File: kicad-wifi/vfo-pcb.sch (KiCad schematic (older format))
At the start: 89 parts, among them J1 Rotery Encoder1, J10 Link-out 1-2, J11 Link-out 1-0, J12 Link-out 2-0, J13 Link-out 2-2, J14 Link-out 2-1, J15 Link-out 1-1, J2 Rotery Encoder2, J3 Analog in 3-6, J4 RxTx, J5 V12, J6 ESP32L, J7 ESP32R, J8 ILI9341, J9 Conn_01x07_Female, Q1 BFR92, Q2 BFR92, Q3 BFR92, Q4 BFR92, Q5 BFR92, Q6 BFR92, SW1 Rotary_Encoder_Switch, U1 AMS1117, U2 LM2576HVS-ADJ, U3 Si5351A-B-GT, U4 Si5351A-B-GT, Y1 Crystal, Y2 Crystal

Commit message: update wifi pcb
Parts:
- removed R21, R22, R23, R24, R25, R29: 150, Resistor_SMD:R_1206_3216Metric_Pad1.42x1.75mm_HandSolder, symbol Device:R
- added C20, C21, C22, C23, C24, C25: 100n, Capacitor_SMD:C_1206_3216Metric_Pad1.42x1.75mm_HandSolder, symbol Device:C
- R26, R27, R31: value 33 -> 200
- R33, R34, R37: value 150 -> 68
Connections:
- net at R26.2, R33.1: now also C23.1; no longer J12.1 (In)
- net at R31.2, R37.1: now also C24.1; no longer J14.1 (In)
- net at R28.2, R32.1: now also C20.1; no longer J11.1 (In)
- net at R35.2, R38.1: now also C21.1; no longer J15.1 (In)
- net at R30.2, R36.1: now also C22.1; no longer J10.1 (In)
- net at R27.2, R34.1: now also C25.1; no longer J13.1 (In)
- new net: C23.2, J12.1 (In)
- new net: C24.2, J14.1 (In)
- new net: C20.2, J11.1 (In)
- new net: C21.2, J15.1 (In)
- new net: C22.2, J10.1 (In)
- new net: C25.2, J13.1 (In)
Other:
- moved on the sheet: J10, J11, J12, J13, J14, J15

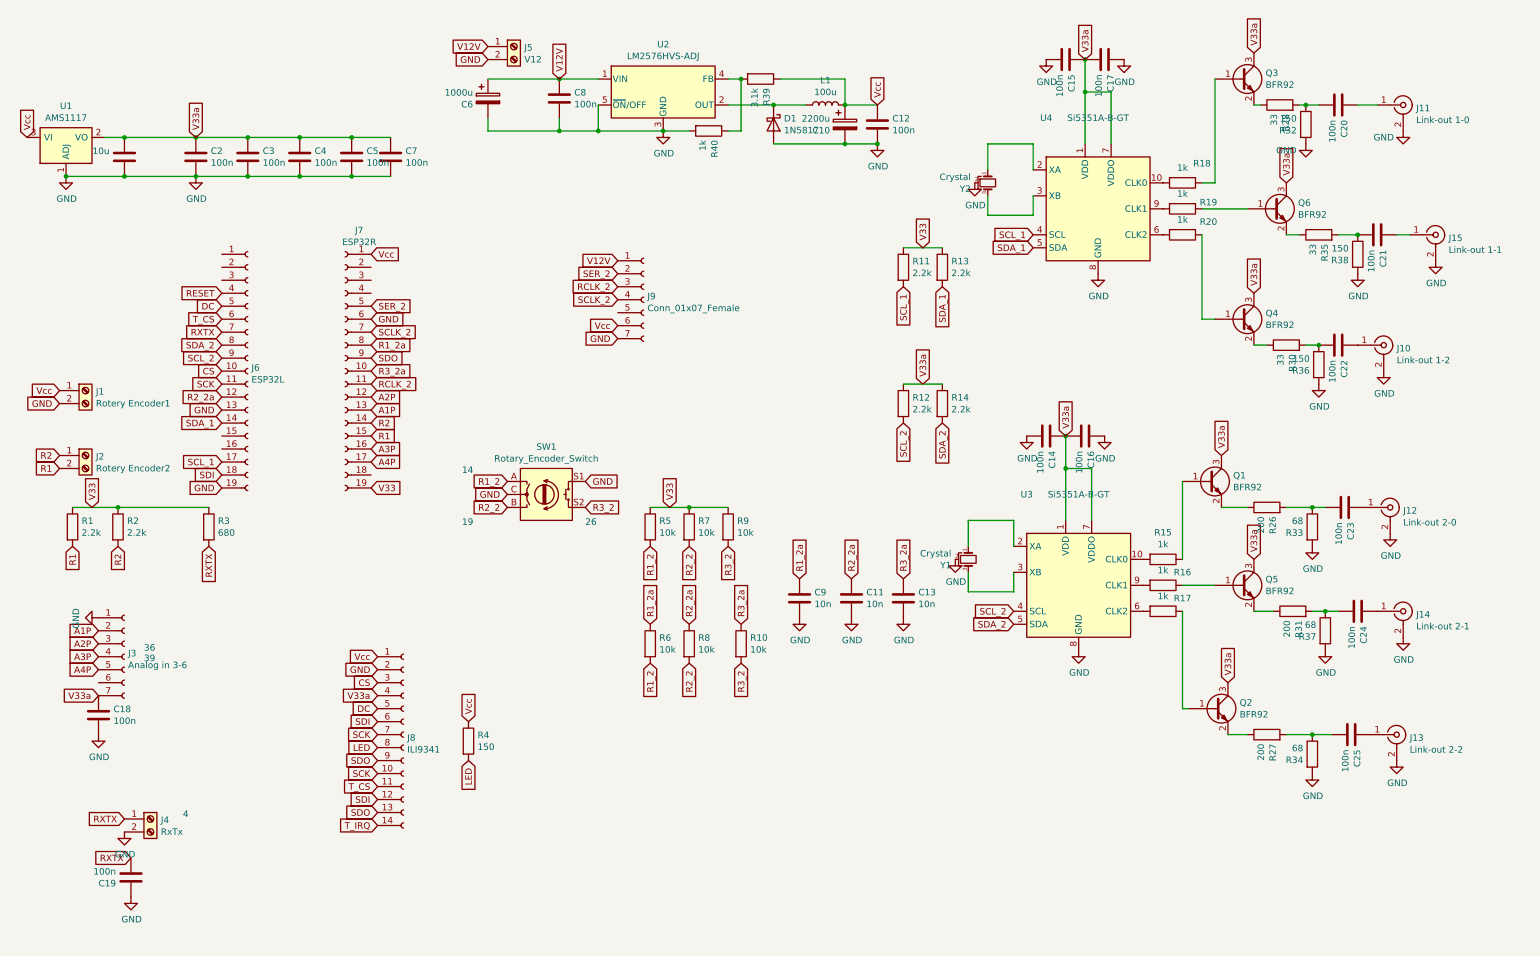
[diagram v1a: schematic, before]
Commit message: jtag interface
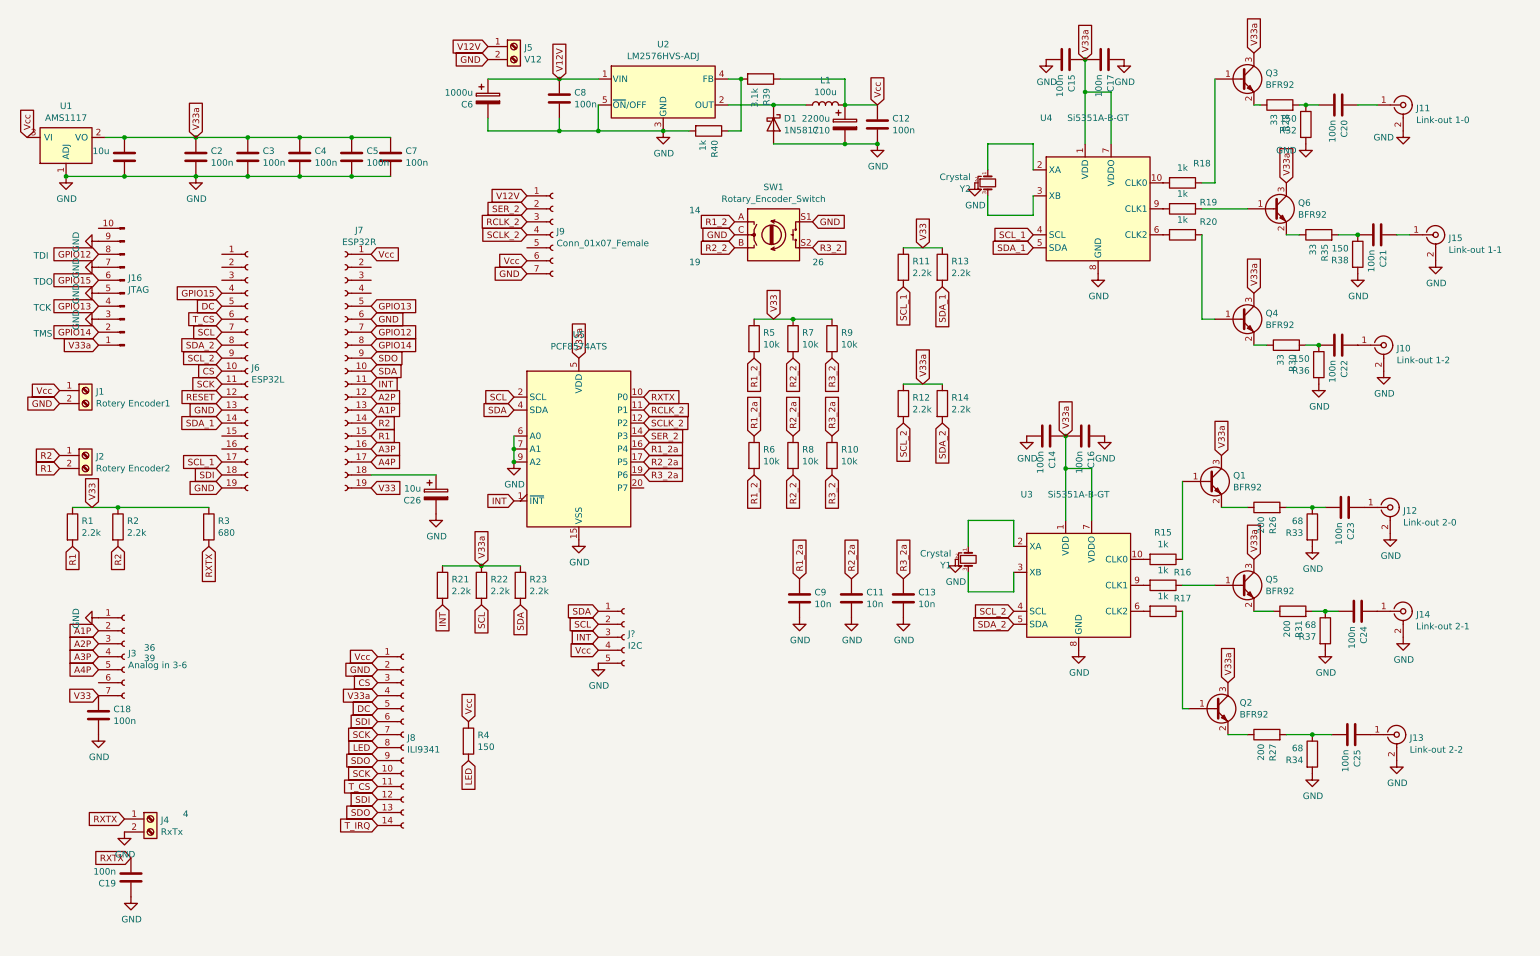
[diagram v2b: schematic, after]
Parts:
- added C26: 10u, Capacitor_SMD:C_1206_3216Metric_Pad1.42x1.75mm_HandSolder, symbol Device:CP
- added J16: JTAG, Connector_PinSocket_2.54mm:PinSocket_2x05_P2.54mm_Vertical, symbol Connector:Conn_01x10_Male
- added J?: I2C, Connector_PinSocket_2.54mm:PinSocket_1x05_P2.54mm_Vertical, symbol Connector:Conn_01x05_Female
- added R21, R22, R23: 2.2k, Resistor_SMD:R_1206_3216Metric_Pad1.42x1.75mm_HandSolder, symbol Device:R
- added U5: PCF8574ATS, Package_SO:SSOP-20_4.4x6.5mm_P0.65mm, symbol Interface_Expansion:PCF8574ATS
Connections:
- net GND: now also C26.2, J16.3 (Pin_3), J16.5 (Pin_5), J16.7 (Pin_7), J16.9 (Pin_9), J?.5 (Pin_5), U5.15 (VSS), U5.6 (A0), U5.7 (A1), U5.9 (A2)
- net R1_2a: now also U5.16 (P4); no longer J7.8 (Pin_8)
- net R2_2a: now also U5.17 (P5); no longer J6.12 (Pin_12)
- net R3_2a: now also U5.19 (P6); no longer J7.10 (Pin_10)
- net RCLK_2: now also U5.11 (P1); no longer J7.11 (Pin_11)
- net RESET: now also J6.12 (Pin_12); no longer J6.4 (Pin_4)
- net RXTX: now also U5.10 (P0); no longer J6.7 (Pin_7)
- net SCLK_2: now also U5.12 (P2); no longer J7.7 (Pin_7)
- net SER_2: now also U5.14 (P3); no longer J7.5 (Pin_5)
- net V33: now also C18.2, J3.7 (Pin_7)
- net V33a: now also J16.1 (Pin_1), R21.1, R22.1, R23.1, U5.5 (VDD); no longer C18.2, J3.7 (Pin_7)
- net Vcc: now also J?.4 (Pin_4)
- net at J7.18 (Pin_18): now also C26.1
- new net GPIO12: J16.8 (Pin_8), J7.7 (Pin_7)
- new net GPIO13: J16.4 (Pin_4), J7.5 (Pin_5)
- new net GPIO14: J16.2 (Pin_2), J7.8 (Pin_8)
- new net GPIO15: J16.6 (Pin_6), J6.4 (Pin_4)
- new net INT: J7.11 (Pin_11), J?.3 (Pin_3), R21.2, U5.1 (~INT~)
- new net SCL: J6.7 (Pin_7), J?.2 (Pin_2), R22.2, U5.2 (SCL)
- new net SDA: J7.10 (Pin_10), J?.1 (Pin_1), R23.2, U5.4 (SDA)
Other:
- note added: "TCK"
- note added: "TDI"
- note added: "TDO"
- note added: "TMS"
- moved on the sheet: J9, R10, R5, R6, R7, R8, R9, SW1

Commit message: 4 layer PCB
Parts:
- removed C18, C2: 100n, Capacitor_SMD:C_1206_3216Metric_Pad1.42x1.75mm_HandSolder, symbol Device:C
- removed J1: Rotery Encoder1, TerminalBlock_MetzConnect:TerminalBlock_MetzConnect_Type011_RT05502HBWC_1x02_P5.00mm_Horizontal, symbol Connector:Screw_Terminal_01x02
- removed J16: JTAG, Connector_PinSocket_2.54mm:PinSocket_2x05_P2.54mm_Vertical, symbol Connector:Conn_01x10_Male
- removed J2: Rotery Encoder2, TerminalBlock_MetzConnect:TerminalBlock_MetzConnect_Type011_RT05502HBWC_1x02_P5.00mm_Horizontal, symbol Connector:Screw_Terminal_01x02
- removed J4: RxTx, TerminalBlock_MetzConnect:TerminalBlock_MetzConnect_Type011_RT05502HBWC_1x02_P5.00mm_Horizontal, symbol Connector:Screw_Terminal_01x02
- removed J6: ESP32L, Connector_PinSocket_2.54mm:PinSocket_1x19_P2.54mm_Vertical, symbol Connector:Conn_01x19_Female
- removed J7: ESP32R, Connector_PinSocket_2.54mm:PinSocket_1x19_P2.54mm_Vertical, symbol Connector:Conn_01x19_Female
- removed J9: Conn_01x07_Female, Connector_PinSocket_2.54mm:PinSocket_1x07_P2.54mm_Vertical, symbol Connector:Conn_01x07_Female
- removed R21: 2.2k, Resistor_SMD:R_1206_3216Metric_Pad1.42x1.75mm_HandSolder, symbol Device:R
- removed U1: AMS1117, Package_TO_SOT_SMD:SOT-223-3_TabPin2, symbol Regulator_Linear:AMS1117
- removed U5: PCF8574ATS, Package_SO:SSOP-20_4.4x6.5mm_P0.65mm, symbol Interface_Expansion:PCF8574ATS
- added C13, C25, C26, C27, C28, C29, C31: 100n, Capacitor_SMD:C_1206_3216Metric_Pad1.42x1.75mm_HandSolder, symbol Device:C
- added C32: 10u, Capacitor_SMD:C_1206_3216Metric_Pad1.42x1.75mm_HandSolder, symbol Device:C
- added J14: Encoders, Connector_PinSocket_2.54mm:PinSocket_1x07_P2.54mm_Vertical, symbol Connector:Conn_01x07_Male
- added J4: Jtag, Connector_PinSocket_2.54mm:PinSocket_2x05_P2.54mm_Vertical, symbol Connector_Generic:Conn_02x05_Odd_Even
- added J6: Prog, Connector_PinSocket_2.54mm:PinSocket_2x03_P2.54mm_Vertical, symbol Connector_Generic:Conn_02x03_Odd_Even
- added R37: 1k, Resistor_SMD:R_1206_3216Metric_Pad1.42x1.75mm_HandSolder, symbol Device:R
- added U3: TCA9548APWR, Package_SO:TSSOP-24_4.4x7.8mm_P0.65mm, symbol Interface_Expansion:TCA9548APWR
- added U5: ESP32-WROOM-32D, RF_Module:ESP32-WROOM-32, symbol RF_Module:ESP32-WROOM-32D
- added U6: LM1117-3.3, Package_TO_SOT_SMD:SOT-223-3_TabPin2, symbol Regulator_Linear:LM1117-3.3
- C20: renamed from C9; value 10n -> 100n
- C21: renamed from C11; value 10n -> 100n
- C22: renamed from C13; value 10n -> 100n
- J10: renamed from J?; footprint Connector_PinSocket_2.54mm:PinSocket_1x05_P2.54mm_Vertical -> Connector_PinSocket_2.54mm:PinSocket_1x07_P2.54mm_Vertical; symbol Connector:Conn_01x05_Female -> Connector:Conn_01x07_Male
- R15: renamed from R30; value 33 -> 200
- R16: renamed from R36; value 150 -> 68
- R2: renamed from R28; value 33 -> 200
- R3: renamed from R32; value 150 -> 68
- R8: renamed from R35; value 33 -> 200
- R9: renamed from R38; value 150 -> 68
- renumbered C15 to C1, C4 to C10, C5 to C11, C7 to C12, C21 to C14, C22 to C15, C14 to C16, C16 to C17, C26 to C18, C23 to C19, C17 to C2, C24 to C23, C25 to C24, C6 to C3, C19 to C30, C8 to C4, C20 to C5, C10 to C6, C12 to C7, C1 to C8, C3 to C9, J5 to J1, J3 to J11, J8 to J12, J11 to J2, J15 to J3, J10 to J5, J12 to J8, J14 to J9, Q3 to Q1, Q6 to Q2, Q4 to Q3, Q1 to Q4, Q2 to Q6, R39 to R1, R11 to R10, R13 to R11, R5 to R12, R7 to R13, R9 to R14, R12 to R17, R14 to R18, R6 to R19, R8 to R20, R10 to R21, R26 to R22, R1 to R23, R2 to R24, R3 to R25, R33 to R26, R15 to R27, R22 to R28, R23 to R29, R16 to R30, R17 to R31, R31 to R32, R37 to R33, R27 to R34, R4 to R35, R34 to R36, R40 to R4, R18 to R5, R19 to R6, R20 to R7, U2 to U1, U4 to U2, U3 to U4, Y2 to Y1, Y1 to Y2
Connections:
- net V33a is gone; now on net V33: C1.2, C10.2, C11.2, C12.2, C16.2, C17.1, C2.1, C8.1, C9.2, J12.4 (Pin_4), Q1.3 (C), Q2.3 (C), Q3.3 (C), Q4.3 (C), Q5.3 (C), Q6.3 (C), R17.1, R18.1, R28.1, R29.1, U2.1 (VDD), U2.7 (VDDO), U4.1 (VDD), U4.7 (VDDO)
- net A1P: now also C28.2, U5.8 (IO32)
- net A2P: now also C29.2, U5.9 (IO33)
- net A3P: now also C27.2, U5.5 (SENSOR_VN)
- net A4P: now also C26.2, U5.4 (SENSOR_VP)
- net CS: now also U5.29 (IO5)
- net DC: now also U5.24 (IO2)
- net GND: now also J10.7 (Pin_7), C13.1, C25.1, C26.1, C27.1, C28.1, C29.1, C31.1, C32.2, J14.2 (Pin_2), J14.6 (Pin_6), J4.1 (Pin_1), J4.3 (Pin_3), J4.5 (Pin_5), J6.3 (Pin_3), U3.1 (A0), U3.12 (GND), U3.2 (A1), U3.21 (A2), U3.3 (~RESET), U5.1 (GND), U5.15 (GND), U5.38 (GND), U5.39 (GND), U6.1 (GND); no longer J10.5 (Pin_5)
- net GPIO12: now also J4.4 (Pin_4), U5.14 (IO12)
- net GPIO13: now also J4.8 (Pin_8), U5.16 (IO13)
- net GPIO14: now also J4.10 (Pin_10), U5.13 (IO14)
- net GPIO15: now also J4.6 (Pin_6), U5.23 (IO15)
- net R1: now also J14.3 (Pin_3), U5.33 (IO21)
- net R1_2a: now also U5.27 (IO16)
- net R2: now also J14.4 (Pin_4), U5.7 (IO35)
- net R2_2a: now also U5.28 (IO17)
- net R3_2a: now also U5.36 (IO22)
- net RXTX: now also J14.5 (Pin_5), U5.10 (IO25)
- net SCK: now also U5.30 (IO18)
- net SCL: now also U3.22 (SCL), U5.26 (IO4); no longer J10.2 (Pin_2)
- net SCL_1: now also U3.5 (SC0)
- net SCL_2: now also U3.7 (SC1)
- net SDA: now also U3.23 (SDA), U5.11 (IO26); no longer J10.1 (Pin_1)
- net SDA_1: now also U3.4 (SD0)
- net SDA_2: now also U3.6 (SD1)
- net SDI: now also U5.37 (IO23)
- net SDO: now also U5.12 (IO27)
- net T_CS: now also J6.5 (Pin_5), U5.25 (IO0)
- net V33: now also C13.2, C31.2, C32.1, J4.9 (Pin_9), J6.1 (Pin_1), R37.1, U3.24 (VCC), U5.2 (VDD), U6.2 (VO)
- net Vcc: now also J10.6 (Pin_6), J14.1 (Pin_1), U6.3 (VI); no longer J10.4 (Pin_4)
- net EN: now reaches C18.1
- net EN: now also J6.2 (Pin_2), R37.2, U5.3 (EN)
- net A5P: now reaches J11.6 (Pin_6)
- net A5P: now also C25.2, U5.6 (IO34)
- net INT renamed SDA_4
- net SDA_4: now also U3.13 (SD4)
- new net RXD0: J6.6 (Pin_6), U5.34 (RXD0/IO3)
- new net SCL_3: J10.2 (Pin_2), U3.9 (SC2)
- new net SCL_4: J10.4 (Pin_4), U3.14 (SC4)
- new net SDA_3: J10.1 (Pin_1), U3.8 (SD2)
- new net TXD0: J6.4 (Pin_4), U5.35 (TXD0/IO1)
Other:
- moved on the sheet: C18, C20, C21, C22, R19, R20, R21

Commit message: band select fixes
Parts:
- added C33: 100n, Capacitor_SMD:C_1206_3216Metric_Pad1.42x1.75mm_HandSolder, symbol Device:C
- added J7: I2C, Connector_PinSocket_2.54mm:PinSocket_1x07_P2.54mm_Vertical, symbol Connector:Conn_01x07_Male
- C8: value 10u -> 100n
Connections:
- net A1P: now also J7.3 (Pin_3)
- net A2P: now also J7.4 (Pin_4)
- net GND: now also C33.1, J7.7 (Pin_7); no longer U3.3 (~RESET)
- net V33: now also U3.3 (~RESET)
- net Vcc: now also C33.2, J7.6 (Pin_6)
- net GPIO19: now reaches U5.31 (IO19)
- net GPIO19: now also J7.5 (Pin_5)
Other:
- note added: "36\n"
- note added: "39"
- note added: "RCLK 33"
- note added: "SCLK 32"
- note added: "SER 19"
- note removed: "4"
- moved on the sheet: C30
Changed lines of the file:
@@
 Wire Wire Line
 	6150 2800 6450 2800
-Text GLabel 6300 2800 1    50   Input ~ 0
-V33
 Text GLabel 6450 3100 3    50   Input ~ 0
 R2_2
@@
 Text GLabel 6750 3100 3    50   Input ~ 0
 R3_2
-Wire Wire Line
-	6450 2800 6750 2800
 Connection ~ 6450 2800
 $Comp
@@
 	1    0    0    -1
 $EndComp
-Text Notes 3750 7350 0    50   ~ 0
-4
 Text GLabel 2250 2700 0    50   Input ~ 0
 A3P
@@
 L Device:C C30
 U 1 1 5FF4718E
-P 1350 7100
-F 0 "C30" H 1235 7054 50  0000 R CNN
-F 1 "100n" H 1235 7145 50  0000 R CNN
-F 2 "Capacitor_SMD:C_1206_3216Metric_Pad1.42x1.75mm_HandSolder" H 1388 6950 50  0001 C CNN
-F 3 "~" H 1350 7100 50  0001 C CNN
-	1    1350 7100
-	1    0    0    -1
-$EndComp
-Text GLabel 1350 6950 0    50   Input ~ 0
+P 3550 7250
+F 0 "C30" H 3435 7204 50  0000 R CNN
+F 1 "100n" H 3435 7295 50  0000 R CNN
+F 2 "Capacitor_SMD:C_1206_3216Metric_Pad1.42x1.75mm_HandSolder" H 3588 7100 50  0001 C CNN
+F 3 "~" H 3550 7250 50  0001 C CNN
+	1    3550 7250
+	1    0    0    -1
+$EndComp
+Text GLabel 3550 7100 0    50   Input ~ 0
 RXTX
 $Comp
 L power:GND #PWR038
 U 1 1 5FF48F51
-P 1350 7250
-F 0 "#PWR038" H 1350 7000 50  0001 C CNN
-F 1 "GND" H 1355 7077 50  0000 C CNN
-F 2 "" H 1350 7250 50  0001 C CNN
-F 3 "" H 1350 7250 50  0001 C CNN
-	1    1350 7250
+P 3550 7400
+F 0 "#PWR038" H 3550 7150 50  0001 C CNN
+F 1 "GND" H 3555 7227 50  0000 C CNN
+F 2 "" H 3550 7400 50  0001 C CNN
+F 3 "" H 3550 7400 50  0001 C CNN
+	1    3550 7400
 	1    0    0    -1
 $EndComp
@@
 	1    0    0    -1
 $EndComp
-Text GLabel 4700 2500 1    50   Input ~ 0
-V33
 Text GLabel 4300 2700 0    50   Input ~ 0
 SCL
@@
 	1    0    0    -1
 $EndComp
-$Comp
-L Interface_Expansion:TCA9548APWR U3
-U 1 1 608EB6EA
-P 4700 3400
-F 0 "U3" H 4700 4481 50  0000 C CNN
-F 1 "TCA9548APWR" H 4700 4390 50  0000 C CNN
-F 2 "Package_SO:TSSOP-24_4.4x7.8mm_P0.65mm" H 4700 2400 50  0001 C CNN
-F 3 "http://www.ti.com/lit/ds/symlink/tca9548a.pdf" H 4750 3650 50  0001 C CNN
-	1    4700 3400
-	1    0    0    -1
-$EndComp
-Wire Wire Line
-	4300 3700 4300 3200
-Connection ~ 4300 3700
-Wire Wire Line
-	4300 3700 4300 3800
-Connection ~ 4300 3900
-Connection ~ 4300 3800
-Wire Wire Line
-	4300 3800 4300 3900
 $Comp
 L power:GND #PWR023
@@
 P 1300 1550
 F 0 "C8" H 1185 1504 50  0001 R CNN
-F 1 "10u" H 1185 1595 50  0000 R CNN
+F 1 "100n" H 1185 1595 50  0000 R CNN
 F 2 "Capacitor_SMD:C_1206_3216Metric_Pad1.42x1.75mm_HandSolder" H 1338 1400 50  0001 C CNN
 F 3 "~" H 1300 1550 50  0001 C CNN
@@
 Wire Wire Line
 	1650 1700 1850 1700
+$Comp
+L Device:C C33
+U 1 1 60ADEAE7
+P 7450 1300
+F 0 "C33" H 7335 1254 50  0000 R CNN
+F 1 "100n" H 7335 1345 50  0000 R CNN
+F 2 "Capacitor_SMD:C_1206_3216Metric_Pad1.42x1.75mm_HandSolder" H 7488 1150 50  0001 C CNN
+F 3 "~" H 7450 1300 50  0001 C CNN
+	1    7450 1300
+	-1   0    0    1
+$EndComp
+Wire Wire Line
+	7100 1150 7450 1150
+Connection ~ 7100 1150
+Wire Wire Line
+	7450 1450 7100 1450
+Text GLabel 3450 3700 2    50   Input ~ 0
+GPIO19
+Text GLabel 5750 5650 0    50   Input ~ 0
+GPIO19
+$Comp
+L Connector:Conn_01x07_Male J7
+U 1 1 60B4A051
+P 5950 5550
+F 0 "J7" H 5978 5576 50  0000 L CNN
+F 1 "I2C" H 5978 5485 50  0000 L CNN
+F 2 "Connector_PinSocket_2.54mm:PinSocket_1x07_P2.54mm_Vertical" H 5950 5550 50  0001 C CNN
+F 3 "~" H 5950 5550 50  0001 C CNN
+	1    5950 5550
+	-1   0    0    -1
+$EndComp
+Text GLabel 5750 5550 0    50   Input ~ 0
+A2P
+Text GLabel 5750 5450 0    50   Input ~ 0
+A1P
+Text GLabel 5750 5750 0    50   Input ~ 0
+Vcc
+$Comp
+L power:GND #PWR041
+U 1 1 60B4ACCA
+P 5750 5850
+F 0 "#PWR041" H 5750 5600 50  0001 C CNN
+F 1 "GND" H 5755 5677 50  0000 C CNN
+F 2 "" H 5750 5850 50  0001 C CNN
+F 3 "" H 5750 5850 50  0001 C CNN
+	1    5750 5850
+	1    0    0    -1
+$EndComp
+Text GLabel 4300 3200 0    50   Input ~ 0
+V33
+Text Notes 2050 2550 0    50   ~ 0
+36\n
+Text Notes 2050 2850 0    50   ~ 0
+39
+Connection ~ 4300 3800
+Connection ~ 4300 3900
+Wire Wire Line
+	4300 3800 4300 3900
+Wire Wire Line
+	4300 3700 4300 3800
+Wire Wire Line
+	6450 2800 6750 2800
+$Comp
+L Interface_Expansion:TCA9548APWR U3
+U 1 1 608EB6EA
+P 4700 3400
+F 0 "U3" H 4700 4481 50  0000 C CNN
+F 1 "TCA9548APWR" H 4700 4390 50  0000 C CNN
+F 2 "Package_SO:TSSOP-24_4.4x7.8mm_P0.65mm" H 4700 2400 50  0001 C CNN
+F 3 "http://www.ti.com/lit/ds/symlink/tca9548a.pdf" H 4750 3650 50  0001 C CNN
+	1    4700 3400
+	1    0    0    -1
+$EndComp
+Text GLabel 4700 2500 1    50   Input ~ 0
+V33
+Text GLabel 6300 2800 1    50   Input ~ 0
+V33
+Text Notes 5250 5700 0    50   ~ 0
+SER 19
+Text Notes 5250 5600 0    50   ~ 0
+RCLK 33
+Text Notes 5250 5500 0    50   ~ 0
+SCLK 32
 $EndSCHEMATC
